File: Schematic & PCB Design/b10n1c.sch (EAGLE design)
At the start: 54 parts, among them U1 nRF8001, U2 ATMEGA328P-MU, U3 PN532, Y1 16MHz, Y2 32.768, Y3 8MHZ, Y4 27.12MHz

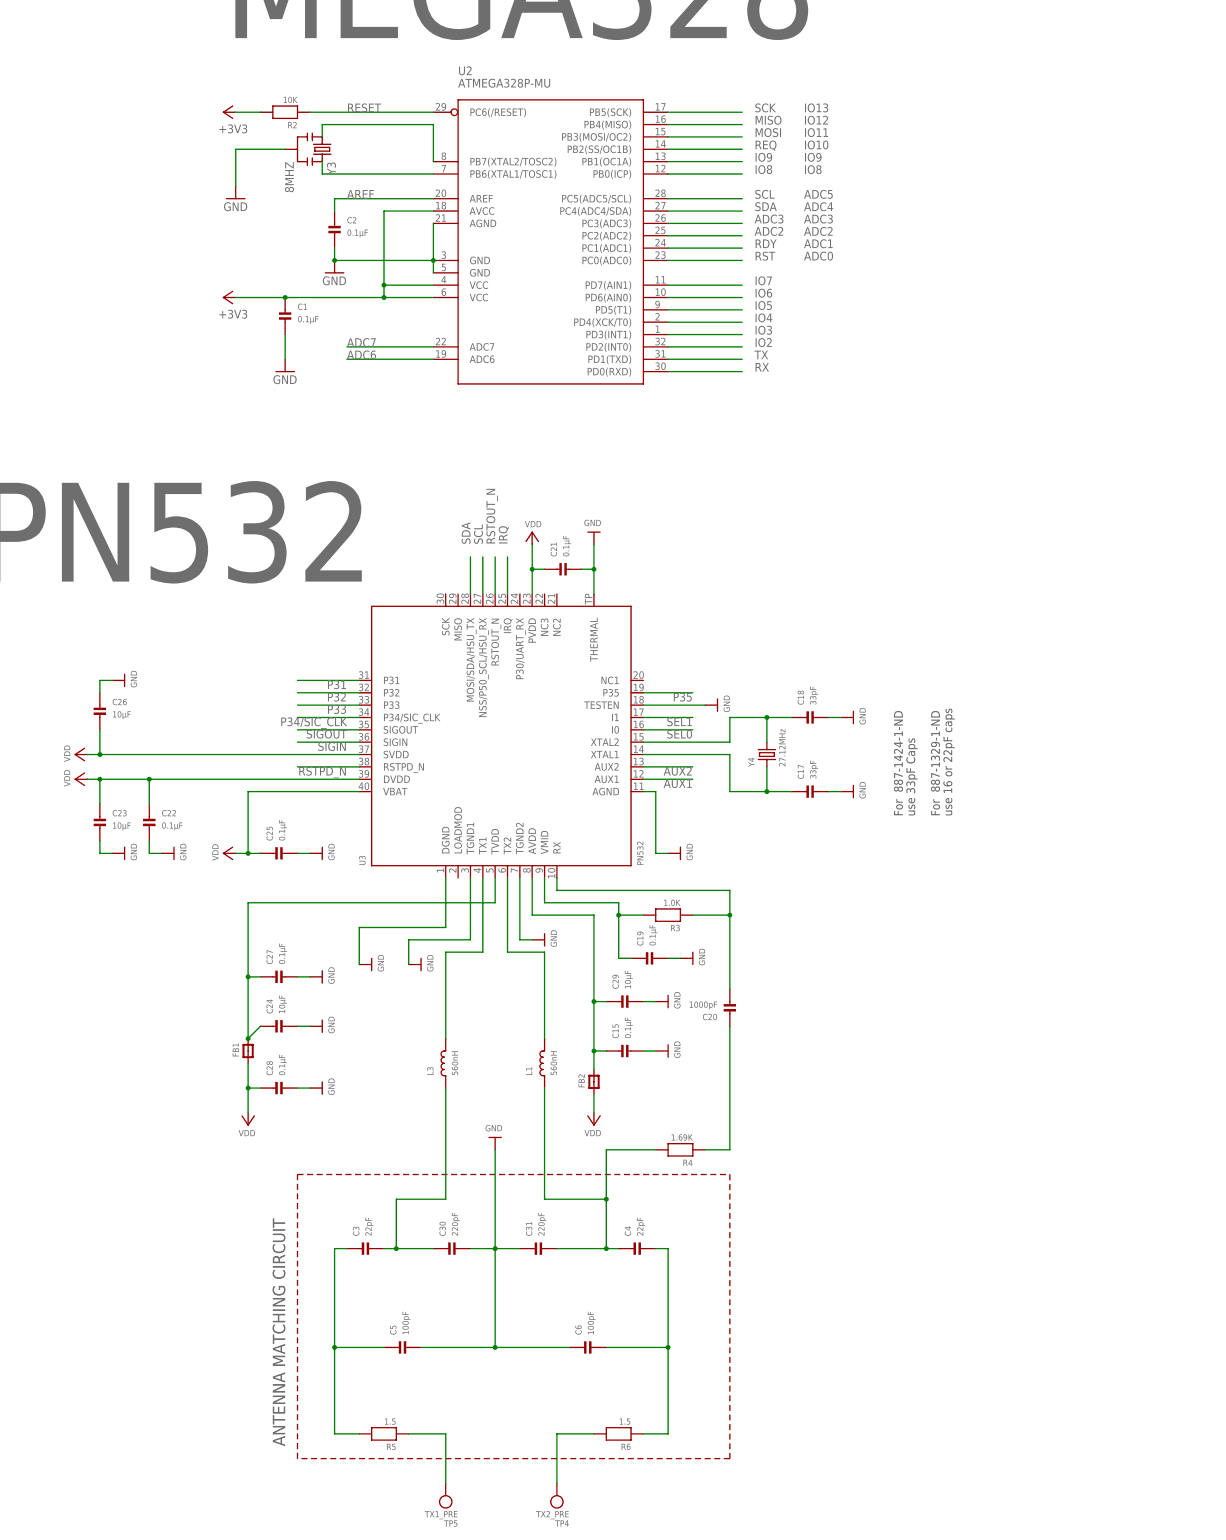
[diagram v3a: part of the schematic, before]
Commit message: PCB and Schem updated, new Eagle libs
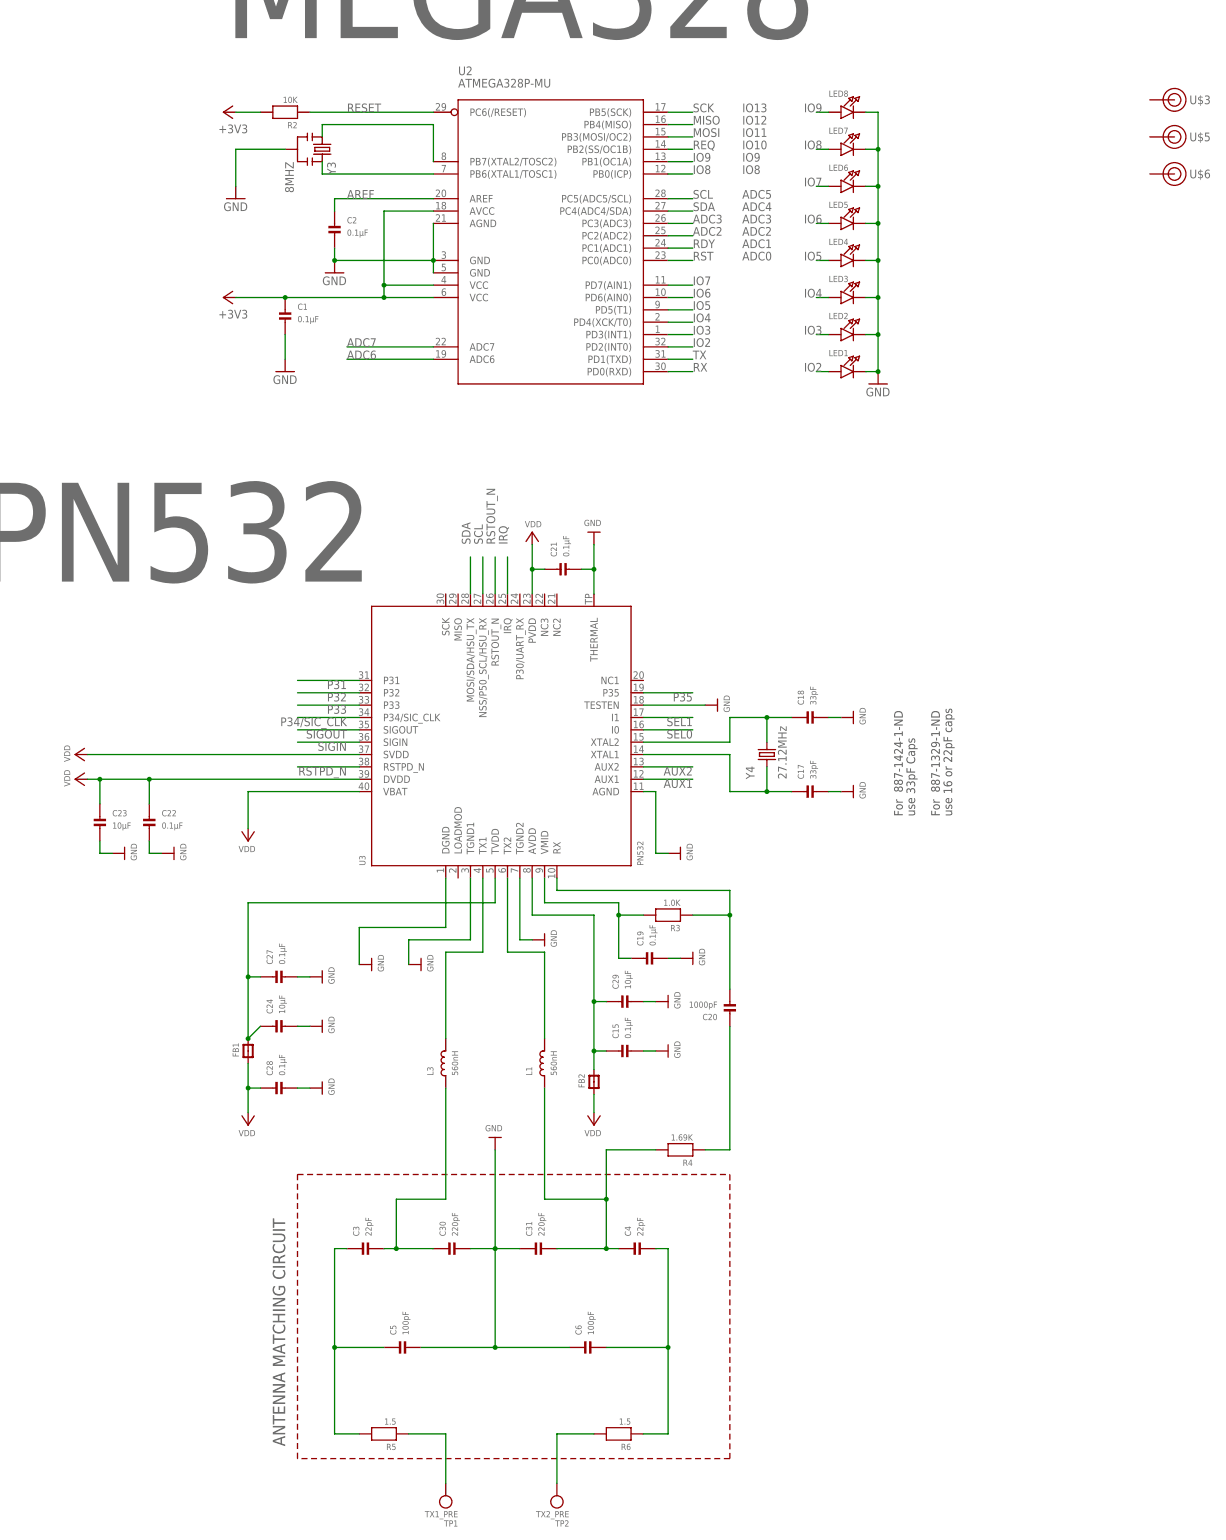
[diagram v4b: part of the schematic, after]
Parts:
- removed C25: 0.1µF, microbuilder:CAP_CERAMIC_0402MP
- removed C26: 10µF, microbuilder:CAP_CERAMIC_0402MP
- removed TP4: TX2_PRE, microbuilder:TESTPOINTPAD
- removed TP5: TX1_PRE, microbuilder:TESTPOINTPAD
- added LED1, LED2, LED3, LED4, LED5, LED6, LED7, LED8: (no value), microbuilder:LED0603_NOOUTLINE
- added TP1: TX1_PRE, microbuilder:TESTPOINTROUND1MM
- added TP2: TX2_PRE, microbuilder:TESTPOINTROUND1MM
- added U$3, U$5, U$6: MAKE-UB312-MICRO, pads-for-MAKE-UB312-micro:MAKE-UB312-MICRO
- Y4: device microbuilder:CRYSTALTHIN -> Crystal-Murata-XRCGB27M120F3M00R0:CRYSTAL
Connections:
- net GND: now also LED1.C, LED2.C, LED3.C, LED4.C, LED5.C, LED6.C, LED7.C, LED8.C; no longer C25.P$2, C26.P$1
- net IO2: now also LED1.A
- net IO3: now also LED2.A
- net IO4: now also LED3.A
- net IO5: now also LED4.A
- net IO6: now also LED5.A
- net IO7: now also LED6.A
- net IO8: now also LED7.A
- net IO9: now also LED8.A
- net N$27: now also TP1.P$1; no longer TP5.P$1
- net N$28: now also TP2.P$1; no longer TP4.P$1
- net VDD: no longer C25.P$1, C26.P$2

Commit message: PN532 PCB layout completed
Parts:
- added C25: 10µF, microbuilder:CAP_CERAMIC_0402MP
- added IC1: BQ51013A, bq500211_bq500210_bq51013a:BQ51013A
- added U5: TLV700XX, WirelessPower:TLV700XX
- C13, C14: value 9pF -> 8pF
- C17, C18: value 33pF -> 8pF
- Y2: DIGIKEY 490-1198-1-ND -> 535-11897-1-ND
- Y4: DIGIKEY (none) -> 490-5581-6-ND
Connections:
- removed net +3V3: C1.P$1, R2.2, U2.AVCC, U2.VCC@1, U2.VCC@2
- removed net IO4: LED3.A, U2.PD4(XCK/T0)
- new net IO10: LED3.A, U2.PB2(SS/OC1B)
- net ADC6: now also LED2.A
- net ADC7: now also LED1.A
- net GND: now also C25.P$2
- net IO2: no longer LED1.A
- net IO3: no longer LED2.A
- net IO5: now also LED8.A; no longer LED4.A
- net IO6: now also LED7.A; no longer LED5.A
- net IO8: now also LED5.A; no longer LED7.A
- net IO9: now also LED4.A; no longer LED8.A
- net IRQ: now also U2.PD4(XCK/T0)
- net REQ: no longer U2.PB2(SS/OC1B)
- net VDD: now also C1.P$1, C25.P$1, R2.2, U2.AVCC, U2.VCC@1, U2.VCC@2
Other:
- note removed: "ADC0"
- note removed: "ADC1"
- note removed: "ADC2"
- note removed: "ADC3"
- note removed: "ADC4"
- note removed: "ADC5"
- note removed: "For 887-1329-1-ND"
- note removed: "For 887-1424-1-ND"
- note removed: "IO10"
- note removed: "IO11"
- note removed: "IO12"
- note removed: "IO13"
- note removed: "IO8"
- note removed: "IO9"
- note removed: "use 16 or 22pF caps"
- note removed: "use 33pF Caps"
- moved on the sheet: C15, C17, C18, C19, C20, C21, C22, C23, C24, C27, C28, C29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

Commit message: bq51013A schematic added
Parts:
- added C26, C32, C33, C34, C35, C36, C37, C38, C39, C40, C41, C42, C43, C44, C45, C46, C47, C48: 0.1µF, microbuilder:CAP_CERAMIC_0402MP
- added R10, R7, R8, R9: 10K, microbuilder:RESISTOR_0402MP
- added TP3, TP4: AC1, microbuilder:TESTPOINTROUND1MM
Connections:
- new net AC1: C32.P$2, C33.P$2, C34.P$2, C44.P$1, C45.P$1, TP3.P$1
- new net AC2: C38.P$1, C39.P$1, C40.P$1, C44.P$2, C45.P$2, IC1G$1.AC2, TP4.P$1
- new net COIL_CHRG_OUT: C46.P$1, C47.P$1, C48.P$1, IC1G$1.OUT, R10.2
- new net N$31: C32.P$1, C33.P$1, C34.P$1, C35.P$2, C36.P$2, C37.P$2, IC1G$1.AC1
- new net N$33: C40.P$2, IC1G$1.BOOT2
- new net N$34: C41.P$2, C42.P$2, C43.P$2, IC1G$1.RECT
- new net N$35: C37.P$1, IC1G$1.BOOT1
- new net N$36: C36.P$1, IC1G$1.CLMP1
- new net N$37: C35.P$1, IC1G$1.COM1
- new net N$38: C39.P$2, IC1G$1.CLMP2
- new net N$39: C38.P$2, IC1G$1.COM2
- new net N$40: IC1G$1.FOD, R7.1, R9.2
- new net N$41: IC1G$1.TS-CTRL, R8.2
- new net N$42: IC1G$1.EN2, R10.1
- new net N$43: IC1G$1.ILIM, R7.2
- net GND: now also C41.P$1, C42.P$1, C43.P$1, C46.P$2, C47.P$2, C48.P$2, IC1G$1.AD, IC1G$1.EN1/TERM, IC1G$1.PGND@1, IC1G$1.PGND@2, IC1G$2.EXP1, IC1G$2.EXP2, IC1G$2.EXP3, IC1G$2.EXP4, IC1G$2.EXP5, IC1G$2.EXP6, IC1G$2.EXP7, R8.1, R9.1
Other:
- note added: "Thermal Pads"
- note added: "[ 5V ]"
- moved on the sheet: U5

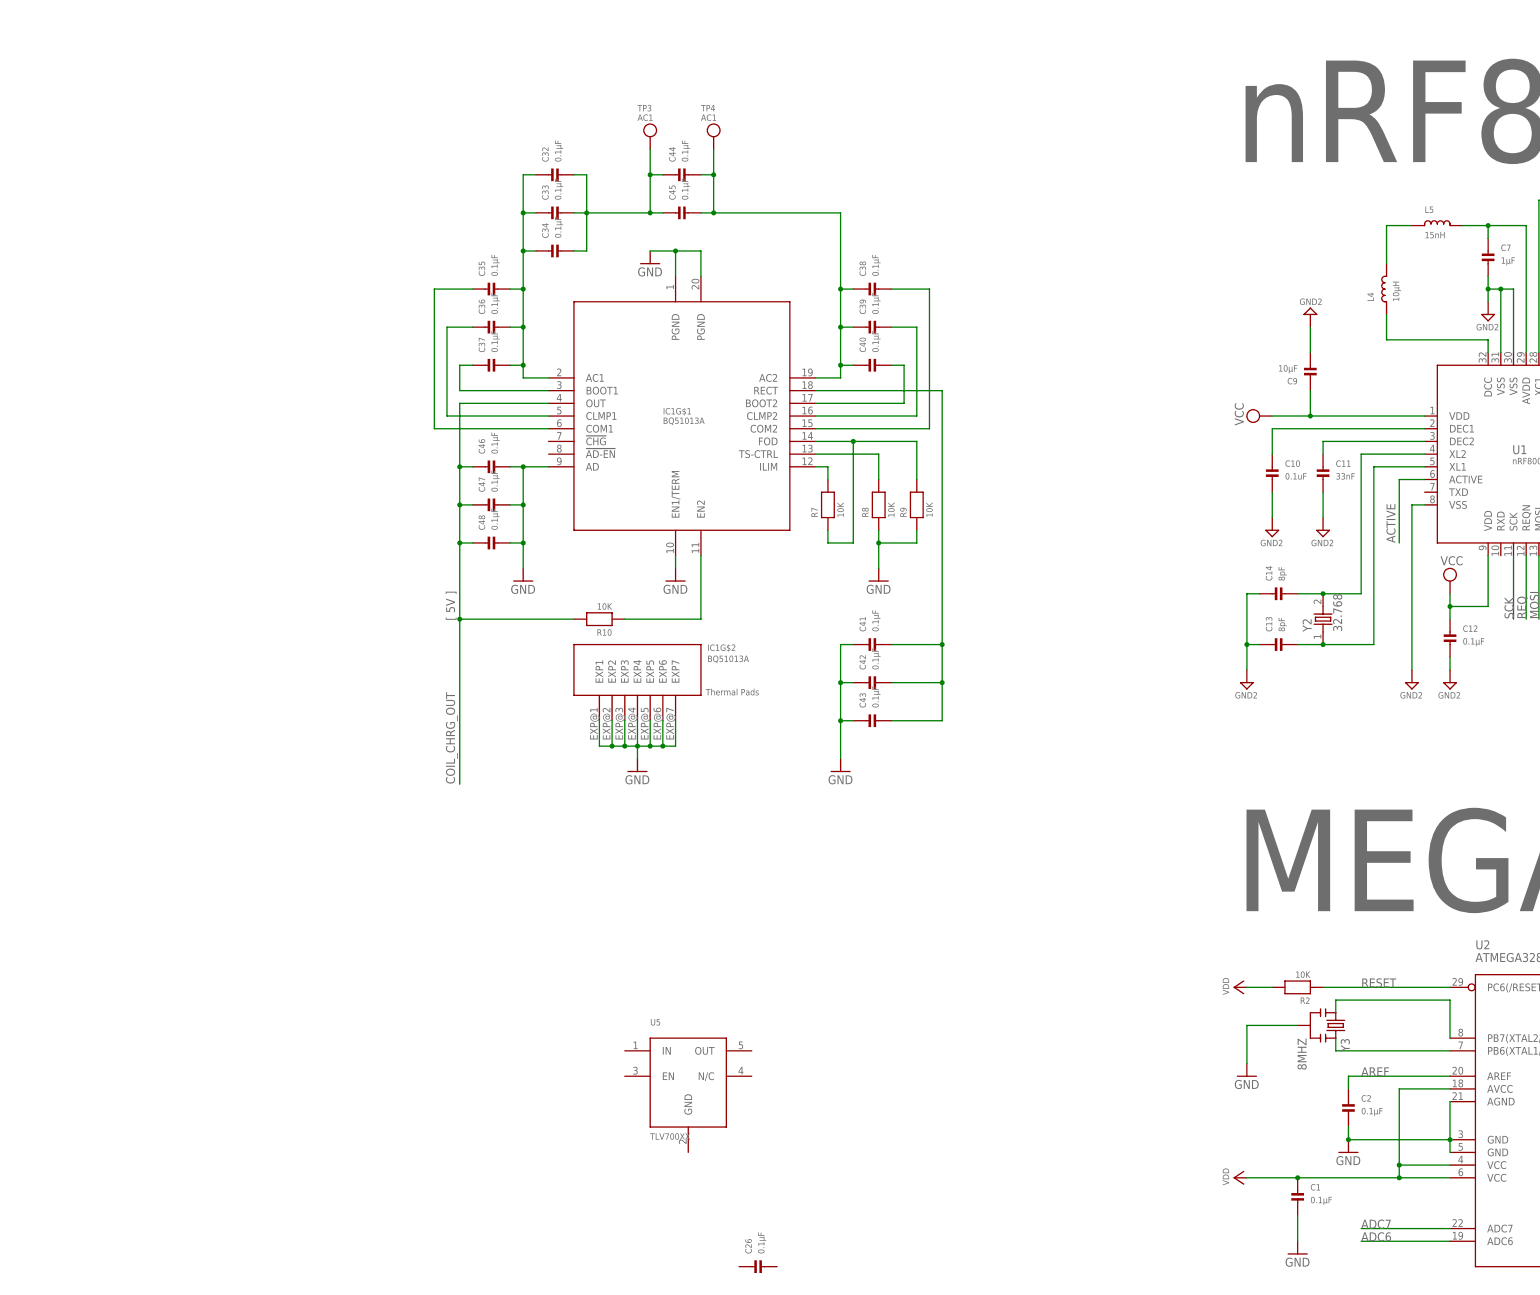
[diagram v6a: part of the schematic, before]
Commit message: Power DONE!
BQ51013 + LTC4065 + MCP1700 schematic and PCB layout DONE
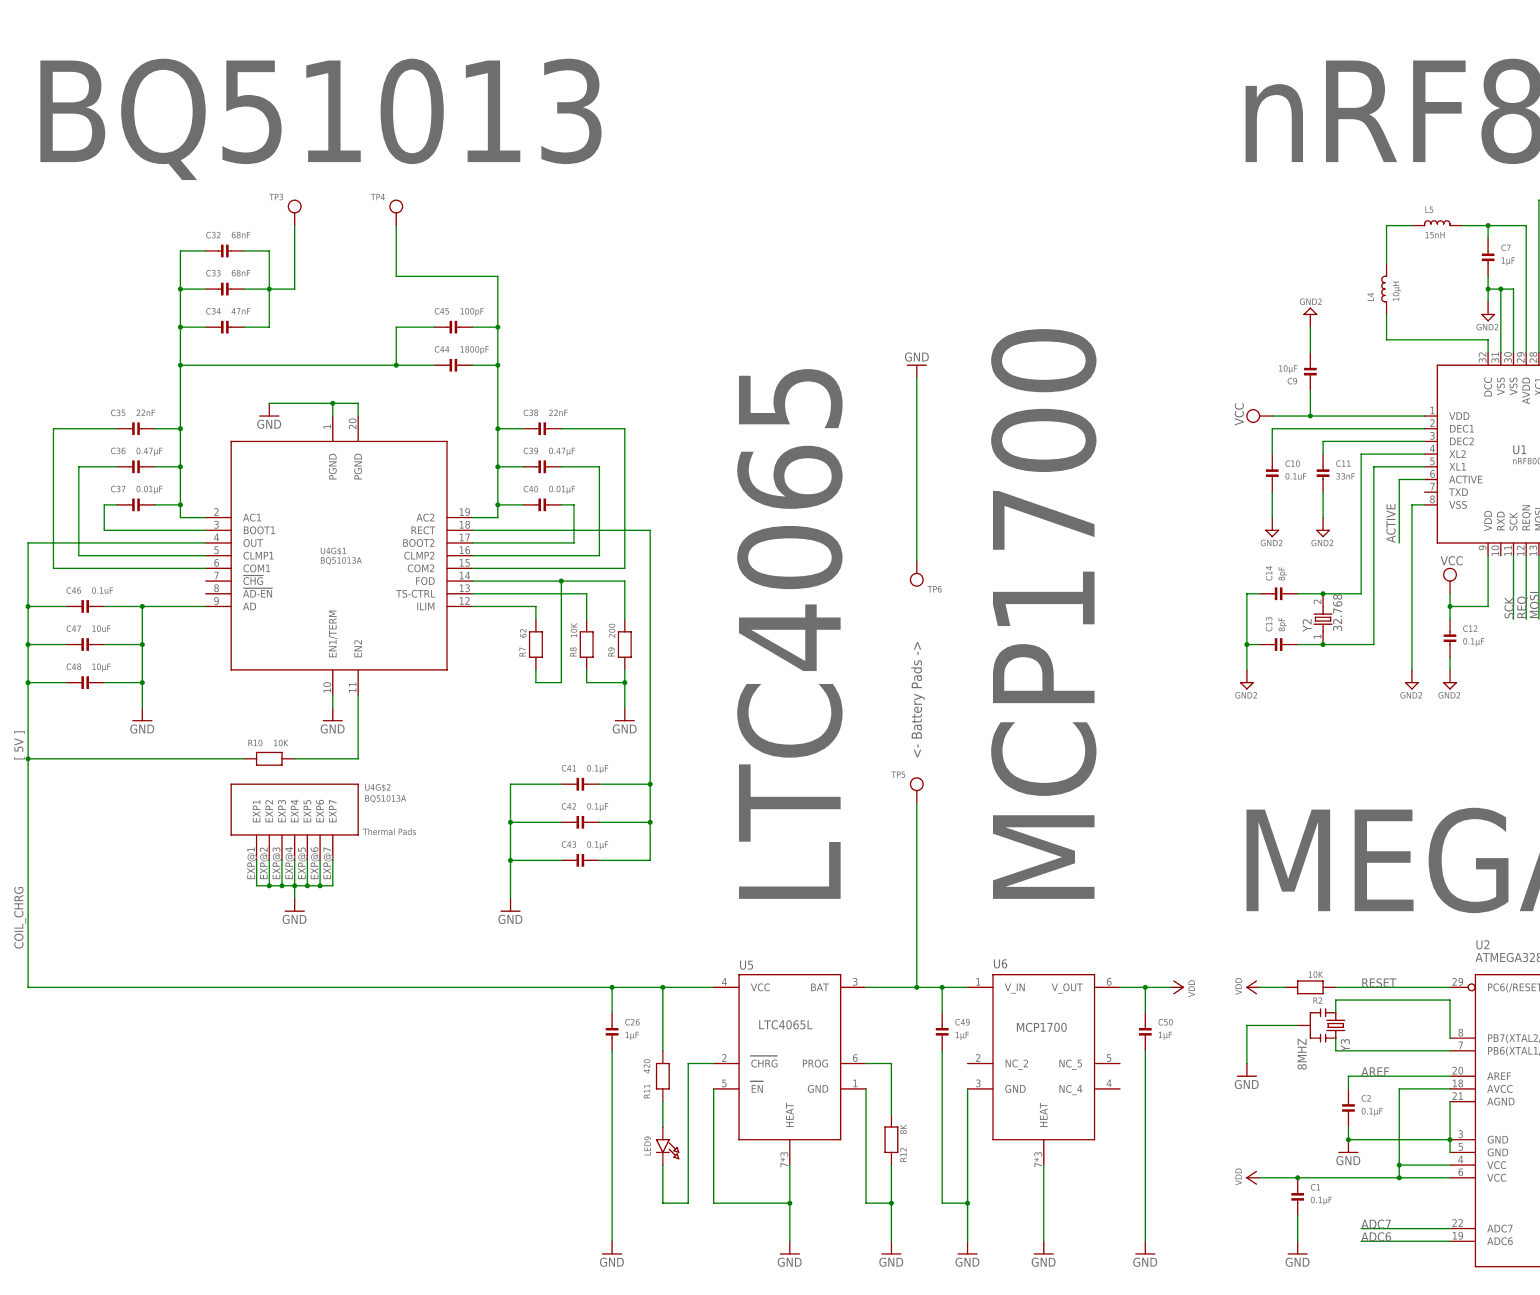
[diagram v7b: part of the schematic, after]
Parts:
- removed IC1: BQ51013A, bq500211_bq500210_bq51013a:BQ51013A
- added C49, C50: 1µF, microbuilder:CAP_CERAMIC_0402MP
- added LED9: (no value), microbuilder:LED0603_NOOUTLINE
- added R11: 420, microbuilder:RESISTOR_0402MP
- added R12: 8K, microbuilder:RESISTOR_0402MP
- added TP5, TP6: (no value), microbuilder:TESTPOINTROUND1MM
- added U4: BQ51013A, bq500211_bq500210_bq51013a:BQ51013A
- added U6: MCP1700, MCP1700:MCP1700
- C26: value 0.1µF -> 1µF
- C32, C33: value 0.1µF -> 68nF
- C34: value 0.1µF -> 47nF
- C35, C38: value 0.1µF -> 22nF
- C36, C39: value 0.1µF -> 0.47µF
- C37, C40: value 0.1µF -> 0.01µF
- C44: value 0.1µF -> 1800pF
- C45: value 0.1µF -> 100pF
- C46: value 0.1µF -> 0.1uF
- C47: value 0.1µF -> 10uF
- C48: value 0.1µF -> 10µF
- R7: value 10K -> 62
- R9: value 10K -> 200
- TP3, TP4: value AC1 -> (none)
- U5: value TLV700XX -> LTC4065L; device WirelessPower:TLV700XX -> LTC4065L:LTC4065L
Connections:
- net GND2 renamed AC
- removed net COIL_CHRG_OUT: C46.P$1, C47.P$1, C48.P$1, IC1G$1.OUT, R10.2
- new net COIL_CHRG: C26.P$1, C46.P$1, C47.P$1, C48.P$1, R10.2, R11.1, U4G$1.OUT, U5.VCC
- new net N$32: LED9.A, R11.2
- new net N$44: LED9.C, U5.CHRG
- new net N$45: R12.1, U5.PROG
- new net N$47: C49.P$1, TP5.P$1, U5.BAT, U6.V_IN
- net AC1: no longer C44.P$1, C45.P$1
- net AC2: now also U4G$1.AC2; no longer IC1G$1.AC2
- net GND: now also C26.P$2, C49.P$2, C50.P$2, R12.2, TP6.P$1, U4G$1.AD, U4G$1.EN1/TERM, U4G$1.PGND@1, U4G$1.PGND@2, U4G$2.EXP1, U4G$2.EXP2, U4G$2.EXP3, U4G$2.EXP4, U4G$2.EXP5, U4G$2.EXP6, U4G$2.EXP7, U5.EN, U5.GND, U5.HEAT, U6.GND, U6.HEAT; no longer IC1G$1.AD, IC1G$1.EN1/TERM, IC1G$1.PGND@1, IC1G$1.PGND@2, IC1G$2.EXP1, IC1G$2.EXP2, IC1G$2.EXP3, IC1G$2.EXP4, IC1G$2.EXP5, IC1G$2.EXP6, IC1G$2.EXP7
- net N$31: now also C44.P$1, C45.P$1, U4G$1.AC1; no longer IC1G$1.AC1
- net N$33: now also U4G$1.BOOT2; no longer IC1G$1.BOOT2
- net N$34: now also U4G$1.RECT; no longer IC1G$1.RECT
- net N$35: now also U4G$1.BOOT1; no longer IC1G$1.BOOT1
- net N$36: now also U4G$1.CLMP1; no longer IC1G$1.CLMP1
- net N$37: now also U4G$1.COM1; no longer IC1G$1.COM1
- net N$38: now also U4G$1.CLMP2; no longer IC1G$1.CLMP2
- net N$39: now also U4G$1.COM2; no longer IC1G$1.COM2
- net N$40: now also U4G$1.FOD; no longer IC1G$1.FOD
- net N$41: now also U4G$1.TS-CTRL; no longer IC1G$1.TS-CTRL
- net N$42: now also U4G$1.EN2; no longer IC1G$1.EN2
- net N$43: now also U4G$1.ILIM; no longer IC1G$1.ILIM
- net VDD: now also C50.P$1, U6.V_OUT
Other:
- note added: "<- Battery Pads ->"
- note added: "BQ51013"
- note added: "LTC4065"
- note added: "MCP1700"
- moved on the sheet: C26, C32, C33, C34, C35, C36, C37, C38, C39, C40, C41, C42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
